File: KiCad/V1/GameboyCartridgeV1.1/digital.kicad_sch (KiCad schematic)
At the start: 29 parts, among them J1 USB_C_Receptacle_USB2.0, J2 DBG_UART, J3 Conn_01x06, SW1 SW_Push, U1 W25Q128JVS, U2 RP2040, Y1 12MHz

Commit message: main changes
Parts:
- C10, C12, C13, C2, C5, C6, C8, C9: renamed from C3; footprint Capacitor_SMD:C_0402_1005Metric_Pad0.74x0.62mm_HandSolder -> Capacitor_SMD:C_0603_1608Metric_Pad1.08x0.95mm_HandSolder
- D1: footprint LED_SMD:LED_WS2812B_PLCC4_5.0x5.0mm_P3.2mm -> LED_SMD:LED_WS2812B-2020_PLCC4_2.0x2.0mm
- SW1: footprint Button_Switch_SMD:SW_SPST_TL3342 -> Button_Switch_SMD:SW_Push_SPST_NO_Alps_SKRK
- renumbered C3 to C1, C3 to C11, C3 to C14, C3 to C4, C3 to C7

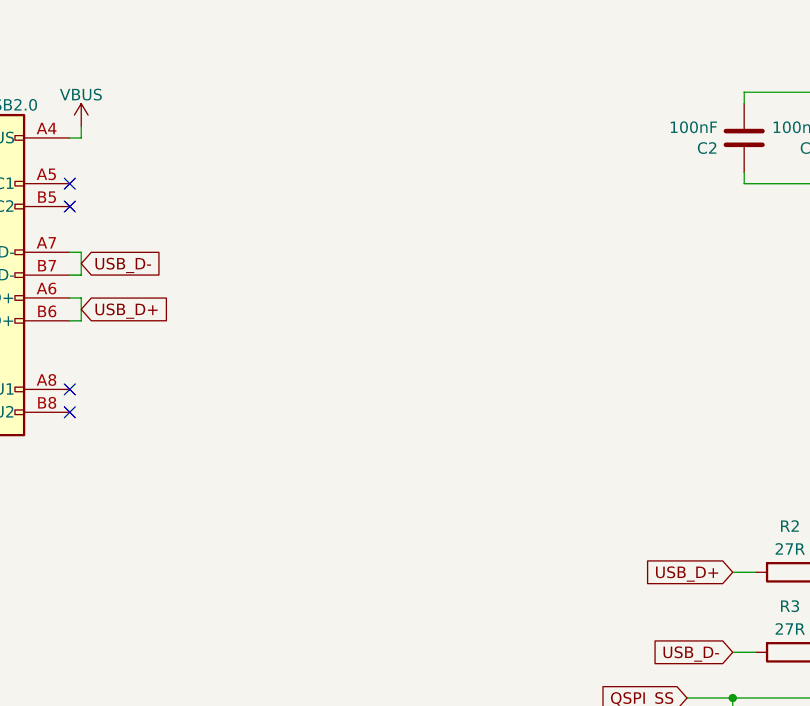
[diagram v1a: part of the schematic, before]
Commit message: usb port placement
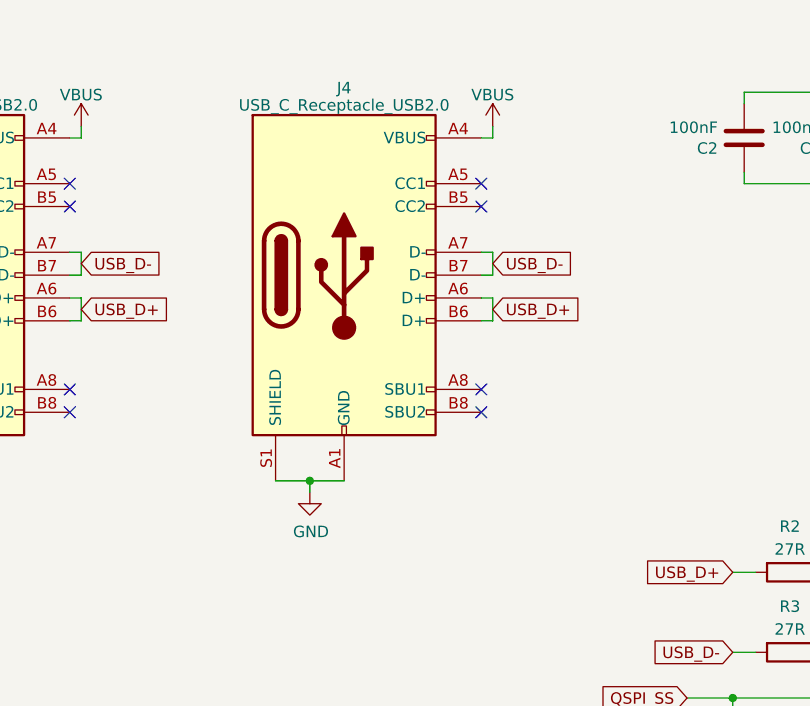
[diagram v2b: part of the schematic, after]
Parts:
- added J4: USB_C_Receptacle_USB2.0, Connector_USB:USB_C_Receptacle_GCT_USB4105-xx-A_16P_TopMnt_Horizontal, symbol Connector:USB_C_Receptacle_USB2.0
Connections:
- net GND: now also J4.A1 (GND), J4.A12 (GND), J4.B1 (GND), J4.B12 (GND), J4.S1 (SHIELD)
- net USB_D+: now also J4.A6 (D+), J4.B6 (D+)
- net USB_D-: now also J4.A7 (D-), J4.B7 (D-)
- net VBUS: now also J4.A4 (VBUS), J4.A9 (VBUS), J4.B4 (VBUS), J4.B9 (VBUS)
- no-connect marks 7 -> 11
